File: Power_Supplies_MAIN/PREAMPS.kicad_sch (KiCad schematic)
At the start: 134 parts, among them J10 XLR3_AudioJack3_Combo, J20 ACJM-MV-2, J29 PINHD_1x2_Female, J3 XLR3_AudioJack3_Combo, J30 PINHD_1x2_Female, J31 PINHD_1x2_Female, J32 PINHD_1x2_Female, J4 XLR3_AudioJack3_Combo, J5 ACJM-MV-2, J6 ACJM-MV-2, J7 ACJM-MV-2, J9 XLR3_AudioJack3_Combo, U15 OPA2134, U16 SSM2019BRNZ, U17 SSM2019BRNZ, U18 OPA2134, U19 SSM2019BRNZ, U20 SSM2019BRNZ

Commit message: stuff i may or may not have done to order these things
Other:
- note added: "+"
- note added: "-"
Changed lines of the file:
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@@
+		)
+	)
+	(text "+"
+		(exclude_from_sim no)
+		(at 98.552 96.266 0)
+		(effects
+			(font
+				(size 1.27 1.27)
+			)
 		)
 	)
@@
 		(effects
 			(font
+				(size 1.27 1.27)
+			)
+		)
+	)
+	(text "-"
+		(exclude_from_sim no)
+		(at 98.806 87.376 0)
+		(effects
+			(font

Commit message: fixed a lot of stuff
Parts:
- removed J29, J30, J31: PINHD_1x2_Female, Connector_PinSocket_2.54mm:PinSocket_1x02_P2.54mm_Vertical, symbol PCM_SL_Pin_Headers:PINHD_1x2_Female
- added J18: PINHD_1x2_Male, Connector_PinHeader_2.54mm:PinHeader_1x02_P2.54mm_Vertical, symbol PCM_SL_Pin_Headers:PINHD_1x2_Male
- J10, J3, J4, J9: footprint Connector_Audio:Jack_XLR-6.35mm_Neutrik_NCJ6FA-H_Horizontal -> Connector_Audio:Jack_XLR-6.35mm_Neutrik_NCJ6FA-V_Vertical
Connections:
- net 36V: now also R54.2, R56.2, R82.2
- net AGND: now also J18.2
- net AIN_4: now also J18.1

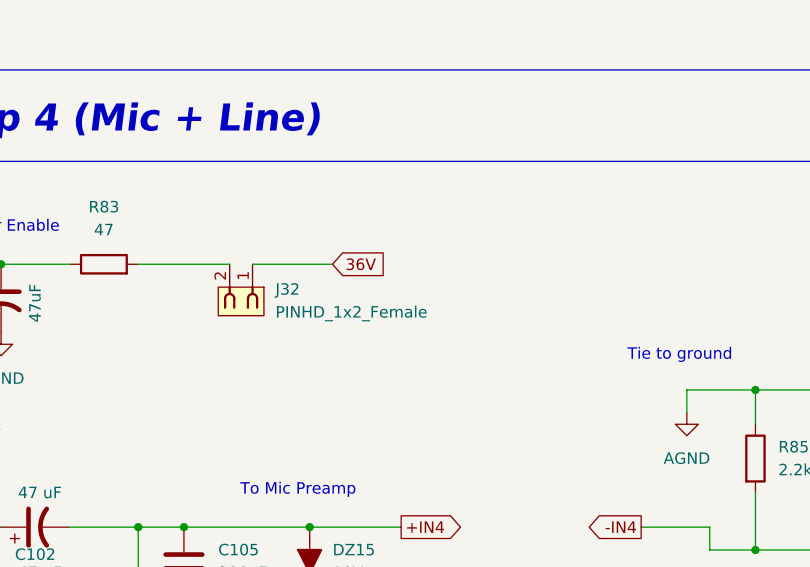
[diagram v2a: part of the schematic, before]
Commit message: fixed power board problems/...
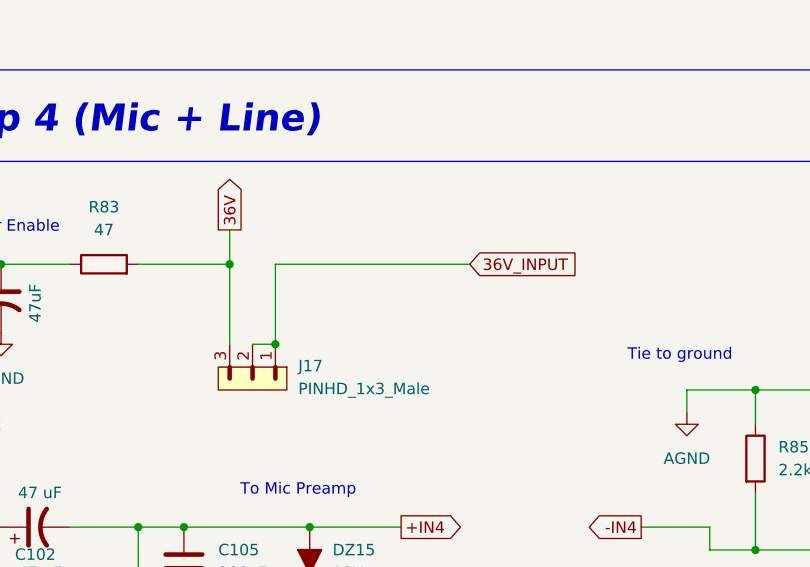
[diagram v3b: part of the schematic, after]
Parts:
- removed J32: PINHD_1x2_Female, Connector_PinSocket_2.54mm:PinSocket_1x02_P2.54mm_Vertical, symbol PCM_SL_Pin_Headers:PINHD_1x2_Female
- added J17: PINHD_1x3_Male, Connector_PinHeader_2.54mm:PinHeader_1x03_P2.54mm_Vertical, symbol PCM_SL_Pin_Headers:PINHD_1x3_Male
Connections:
- net 36V: now also R83.2, J17.3
- new net 36V_INPUT: J17.1, J17.2
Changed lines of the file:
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@@
 	)
 	(junction
+		(at 354.33 177.8)
+		(diameter 0)
+		(color 0 0 0 0)
+	)
+	(junction
 		(at 96.52 365.76)
 		(diameter 0)
@@
 	)
 	(junction
+		(at 349.25 168.91)
+		(diameter 0)
+		(color 0 0 0 0)
+	)
+	(junction
 		(at 143.51 71.12)
 		(diameter 0)
@@
 	(wire
 		(pts
+			(xy 354.33 168.91) (xy 375.92 168.91)
+		)
+		(stroke
+			(width 0)
+			(type default)
+		)
+	)
+	(wire
+		(pts
 			(xy 163.83 365.76) (xy 163.83 363.22)
 		)
@@
 	(wire
 		(pts
+			(xy 349.25 168.91) (xy 349.25 177.8)
+		)
+		(stroke
+			(width 0)
+			(type default)
+		)
+	)
+	(wire
+		(pts
 			(xy 506.73 217.17) (xy 505.46 217.17)
 		)
@@
 	(wire
 		(pts
+			(xy 354.33 177.8) (xy 354.33 168.91)
+		)
+		(stroke
+			(width 0)
+			(type default)
+		)
+	)
+	(wire
+		(pts
 			(xy 41.91 247.65) (xy 48.26 247.65)
 		)
@@
 	(wire
 		(pts
+			(xy 349.25 165.1) (xy 349.25 168.91)
+		)
+		(stroke
+			(width 0)
+			(type default)
+		)
+	)
+	(wire
+		(pts
 			(xy 408.94 72.39) (xy 422.91 72.39)
 		)
@@
 	(wire
 		(pts
-			(xy 351.79 168.91) (xy 360.68 168.91)
-		)
-		(stroke
-			(width 0)
-			(type default)
-		)
-	)
-	(wire
-		(pts
 			(xy 80.01 205.74) (xy 80.01 207.01)
 		)
@@
 	(wire
 		(pts
+			(xy 351.79 177.8) (xy 354.33 177.8)
+		)
+		(stroke
+			(width 0)
+			(type default)
+		)
+	)
+	(wire
+		(pts
 			(xy 26.67 309.88) (xy 26.67 307.34)
 		)
@@
 		)
 	)
-	(global_label "36V"
+	(global_label "36V_INPUT"
 		(shape input)
-		(at 360.68 168.91 0)
+		(at 375.92 168.91 0)
 		(fields_autoplaced yes)
 		(effects
@@
 		)
 		(property "Intersheetrefs" "${INTERSHEET_REFS}"
-			(at 367.1728 168.91 0)
+			(at 388.8838 168.91 0)
 			(effects
 				(font
@@
 		)
 	)
+	(global_label "36V"
+		(shape output)
+		(at 349.25 165.1 90)
+		(fields_autoplaced yes)
+		(effects
+			(font
+				(size 1.27 1.27)
+			)
+			(justify left)
+		)
+		(property "Intersheetrefs" "${INTERSHEET_REFS}"
+			(at 349.25 158.6072 90)
+			(effects
+				(font
+					(size 1.27 1.27)
+				)
+				(justify left)
+				(hide yes)
+			)
+		)
+	)
 	(global_label "12V"
 		(shape input)
@@
 	)
 	(symbol
+		(lib_id "PCM_SL_Pin_Headers:PINHD_1x3_Male")
+		(at 351.79 181.61 270)
+		(unit 1)
+		(exclude_from_sim no)
+		(in_bom yes)
+		(on_board yes)
+		(dnp no)
+		(fields_autoplaced yes)
+		(property "Reference" "J17"
+			(at 356.87 180.2149 90)
+			(effects
+				(font
+					(size 1.27 1.27)
+				)
+				(justify left)
+			)
+		)
+		(property "Value" "PINHD_1x3_Male"
+			(at 356.87 182.7549 90)
+			(effects
+				(font
+					(size 1.27 1.27)
+				)
+				(justify left)
+			)
+		)
+		(property "Footprint" "Connector_PinHeader_2.54mm:PinHeader_1x03_P2.54mm_Vertical"
+			(at 346.71 182.88 0)
+			(effects
+				(font
+					(size 1.27 1.27)
+				)
+				(hide yes)
+			)
+		)
+		(property "Datasheet" ""
+			(at 360.68 181.61 0)
+			(effects
+				(font
+					(size 1.27 1.27)
+				)
+				(hide yes)
+			)
+		)
+		(property "Description" "Pin Header male with pin space 2.54mm. Pin Count -3"
+			(at 351.79 181.61 0)
+			(effects
+				(font
+					(size 1.27 1.27)
+				)
+				(hide yes)
+			)
+		)
+		(pin "3"
+		)
+		(pin "2"
+		)
+		(pin "1"
+		)
+		(instances
+			(project ""
+				(path "/5266cf9e-da90-4c53-80fd-cf3dbed42632/e99ff431-6a4b-4cff-9a72-1b9e305d1dd3"
+					(reference "J17")
+					(unit 1)
+				)
+			)
+		)
+	)
+	(symbol
 		(lib_id "Device:C_Polarized_US")
 		(at 327.66 207.01 90)
@@
 					(unit 1)
 				)
-			)
-		)
-	)
-	(symbol
-		(lib_id "PCM_SL_Pin_Headers:PINHD_1x2_Female")
-		(at 350.52 172.72 270)
-		(unit 1)
-		(exclude_from_sim no)
-		(in_bom yes)
-		(on_board yes)
-		(dnp no)
-		(fields_autoplaced yes)
-		(property "Reference" "J32"
-			(at 354.33 171.7049 90)
-			(effects
-				(font
-					(size 1.27 1.27)
-				)
-				(justify left)
-			)
-		)
-		(property "Value" "PINHD_1x2_Female"
-			(at 354.33 174.2449 90)
-			(effects
-				(font
-					(size 1.27 1.27)
-				)
-				(justify left)
-			)
-		)
-		(property "Footprint" "Connector_PinSocket_2.54mm:PinSocket_1x02_P2.54mm_Vertical"
-			(at 360.68 175.26 0)
-			(effects
-				(font
-					(size 1.27 1.27)
-				)
-				(hide yes)
-			)
-		)
-		(property "Datasheet" ""
-			(at 358.14 172.72 0)
-			(effects
-				(font
-					(size 1.27 1.27)
-				)
-				(hide yes)
-			)
-		)
-		(property "Description" "Pin Header female with pin space 2.54mm. Pin Count -2"
-			(at 350.52 172.72 0)
-			(effects
-				(font
-					(size 1.27 1.27)
-				)
-				(hide yes)
-			)
-		)
-		(pin "1"
-		)
-		(pin "2"
-		)
-		(instances
-			(project "Power_Supplies"
-				(path "/5266cf9e-da90-4c53-80fd-cf3dbed42632/e99ff431-6a4b-4cff-9a72-1b9e305d1dd3"
-					(reference "J32")
-					(unit 1)
-				)
